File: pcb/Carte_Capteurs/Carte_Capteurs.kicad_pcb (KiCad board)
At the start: 2 copper layers, 129.9 x 60 mm, 44 parts, among them J10 DF3A-5P-2DS, J11 DF3A-4P-2DS, J12 DF3A-4P-2DS, J13 Conn_01x02, J5 Conn_02x07_Odd_Even, J6 Molex KK 254, J7 Samtec FTS-105-01-L-DV, J8 Samtec FTS-105-01-L-DV, J9 DF3A-5P-2DS, Q1 NTR3C21NZT1G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

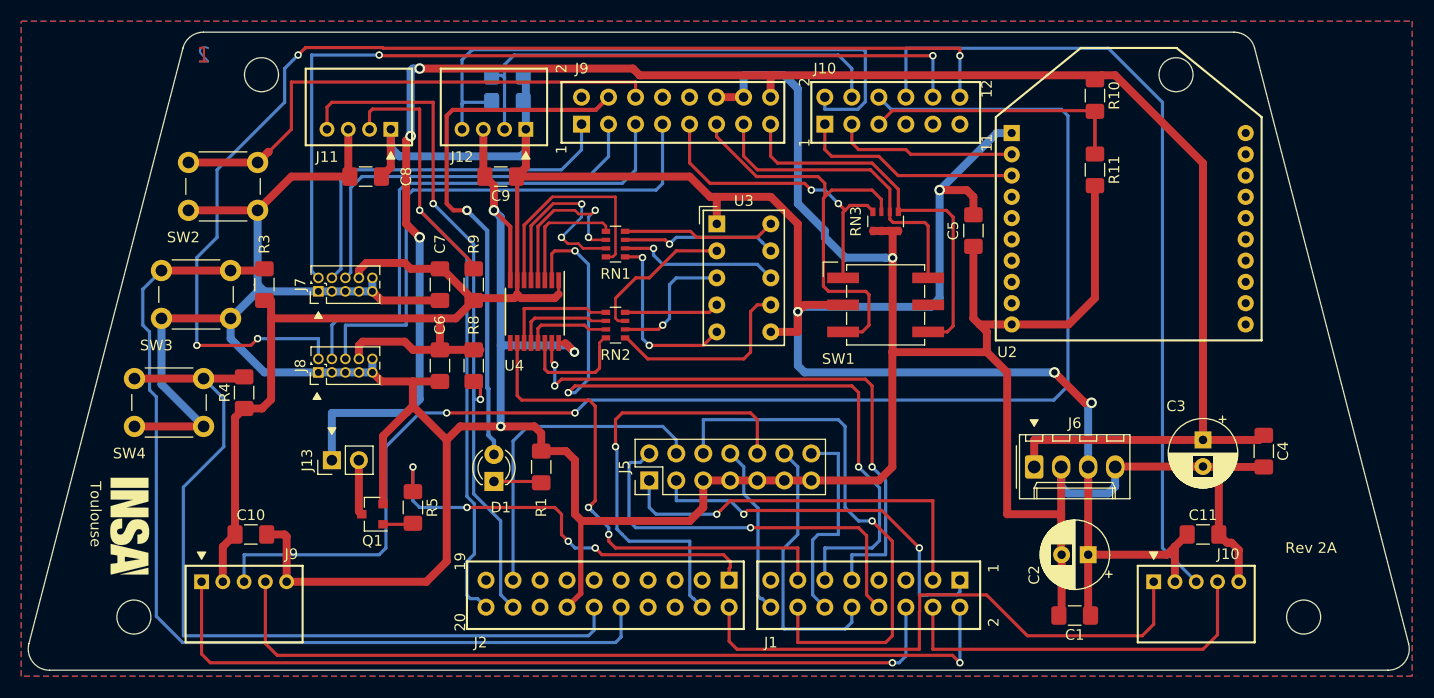
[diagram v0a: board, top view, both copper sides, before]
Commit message: ajout de la carte chassi DFRobotics + creation d'une nouvelle carte led + creation d'une carte capteur pour DFRobotic + correction de l'alimentation en 5V des encodeurs sur DFRobotic (carte Landzo a corriger dans un prochaine commit)
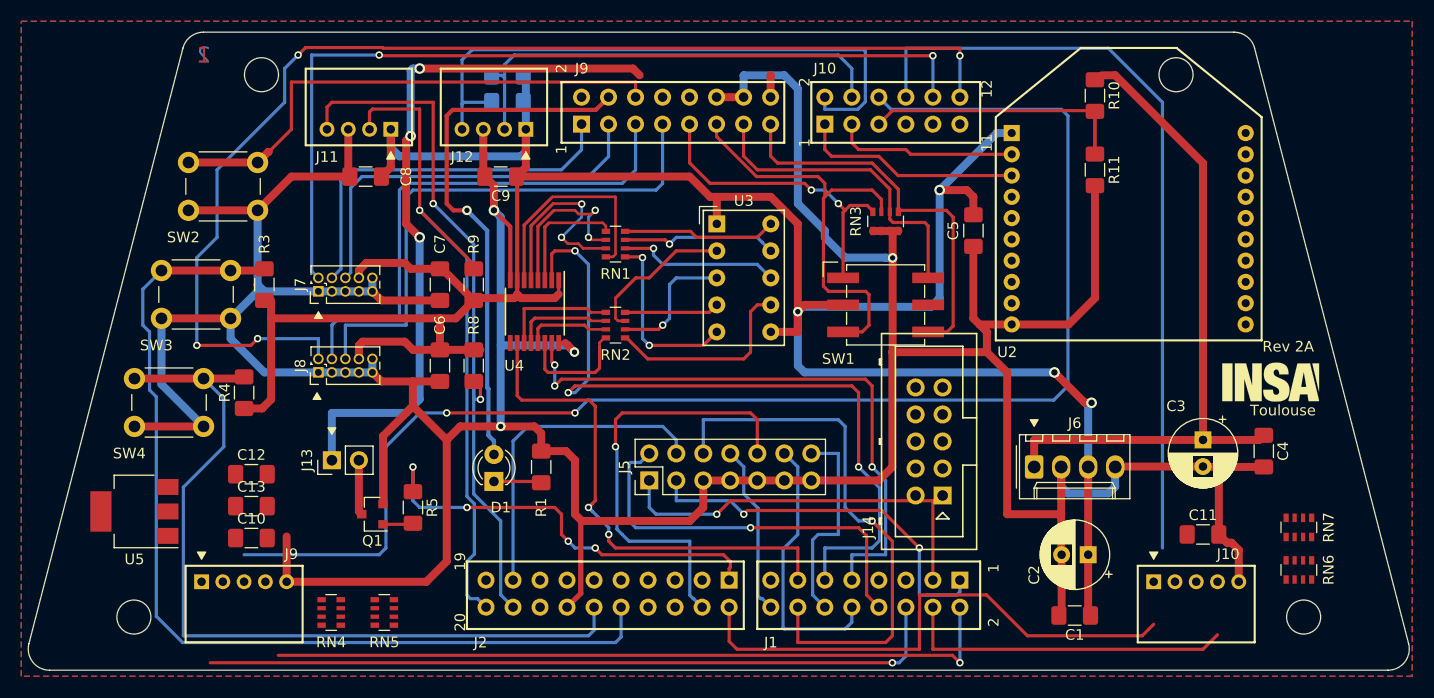
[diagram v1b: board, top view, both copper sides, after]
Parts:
- added C12: 4.7µF, Capacitor_SMD:C_1206_3216Metric_Pad1.42x1.75mm_HandSolder, F.Cu at (108.0, 108.0)
- added C13: 4.7µF, Capacitor_SMD:C_1206_3216Metric_Pad1.42x1.75mm_HandSolder, F.Cu at (108.0, 111.0)
- added J14: Conn_02x05_Odd_Even, Connector_Multicomp:Multicomp_MC9A12-1034_2x05_P2.54mm_Vertical, F.Cu at (173.0, 110.0)
- added RN4: 2.2K, Resistor_SMD:R_Array_Convex_4x0603, F.Cu at (115.5, 121.0)
- added RN5: 3.3K, Resistor_SMD:R_Array_Convex_4x0603, F.Cu at (120.5, 121.0)
- added RN6: 2.2K, Resistor_SMD:R_Array_Convex_4x0603, F.Cu at (206.5, 117.0)
- added RN7: 3.3K, Resistor_SMD:R_Array_Convex_4x0603, F.Cu at (206.5, 113.0)
- added U5: ZLDO1117G50TA, Package_TO_SOT_SMD:SOT-223-3_TabPin2, F.Cu at (97.0, 111.5)
- moved Logo1 108.5 mm to (204.0, 99.5), turned to 0 degrees
- moved C10 0.34 mm to (108.0, 114.0)
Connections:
- C10 pad 1: +3V3 -> +5V
- C11 pad 1: +3V3 -> +5V
- J10 pad 1: /ENC_INDEX2 -> Net-(J10-Pad1)
- J10 pad 2: +3V3 -> +5V
- J10 pad 3: /ENC_SIG_A2 -> Net-(J10-Pad3)
- J10 pad 4: /ENC_SIG_B2 -> Net-(J10-Pad4)
- J9 pad 1: /ENC_INDEX1 -> Net-(J9-Pad1)
- J9 pad 2: +3V3 -> +5V
- J9 pad 3: /ENC_SIG_A1 -> Net-(J9-Pad3)
- J9 pad 4: /ENC_SIG_B1 -> Net-(J9-Pad4)
- U1 pad 1.5: (no net) -> /PIXY2_TX
- U1 pad 1.7: (no net) -> /PIXY2_RX
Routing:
- net +BATT: track 176.3 -> 132.9 mm
- net +3V3: track 285.2 -> 254.7 mm
- net /ENC_INDEX1: track 78.2 -> 70.3 mm
- net /ENC_SIG_B1: track 77.1 -> 69.6 mm
- net /ENC_SIG_B2: track 36.3 -> 31.3 mm
- net /ENC_SIG_A2: track 77.2 -> 72.7 mm
- net /ENC_INDEX2: track 54.6 -> 50.6 mm
- net /ENC_SIG_A1: track 136.1 -> 133.5 mm
- net GND: track 431.6 -> 429.7 mm
